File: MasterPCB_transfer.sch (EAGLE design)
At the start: 1072 parts, among them IC1 NCS21911SN2T1G, IC10 LDL1117S33R, IC11 LTC4222CUH#PBF, IC12 LTC4222CUH#PBF, IC13 LTC4222CUH#PBF, IC14 LTC4222CUH#PBF, IC15 LTC4222CUH#PBF, IC16 LTC4222CUH#PBF, IC17 LTC4222CUH#PBF, IC18 LTC4222CUH#PBF, IC19 LTC4222CUH#PBF, IC2 NCS21911SN2T1G, IC20 LTC4222CUH#PBF, IC21 LTC4222CUH#PBF, IC22 LTC4222CUH#PBF, IC23 LTC4222CUH#PBF, IC24 NCS21911SN2T1G, IC25 NCS21911SN2T1G, IC26 NCS21911SN2T1G, IC27 NCS21911SN2T1G, IC28 NCS21911SN2T1G, IC29 NCS21911SN2T1G, IC3 NCS21911SN2T1G, IC30 NCS21911SN2T1G, IC31 ADIS16500AMLZ, IC32 LTC6820IUD#PBF, IC33 CBTL01023GM,115, IC34 MAX889TESA+, IC35 NCS21911SN2T1G, IC36 NCS21911SN2T1G, IC37 NCS21911SN2T1G, IC38 ADS8588HIPM, IC39 NCS21911SN2T1G, IC4 LTC4222CUH#PBF, IC40 NCS21911SN2T1G, IC41 NCS21911SN2T1G, IC42 NCS21911SN2T1G, IC43 NCS21911SN2T1G, IC44 NCS21911SN2T1G, IC45 NCS21911SN2T1G, IC46 NCS21911SN2T1G, IC47 NCS21911SN2T1G, IC48 NCS21911SN2T1G, IC49 NCS21911SN2T1G, IC5 LP38692SDX-5.0_NOPB, IC50 NCS21911SN2T1G, IC51 ADS8588HIPM, IC52 ADS8588HIPM, IC53 NCS21911SN2T1G, IC54 NCS21911SN2T1G, IC55 NCS21911SN2T1G, IC56 NCS21911SN2T1G, IC57 NCS21911SN2T1G, IC58 NCS21911SN2T1G, IC59 NCS21911SN2T1G, IC6 LP38692SDX-5.0_NOPB, IC60 NCS21911SN2T1G, IC61 NCS21911SN2T1G, IC62 NCS21911SN2T1G, IC63 NCS21911SN2T1G, IC64 NCS21911SN2T1G, IC65 NCS21911SN2T1G, IC66 NCS21911SN2T1G, IC67 NCS21911SN2T1G, IC68 NCS21911SN2T1G, IC69 NCS21911SN2T1G, IC7 LDL1117S33R, IC70 NCS21911SN2T1G, IC71 NCS21911SN2T1G, IC72 NCS21911SN2T1G, IC73 NCS21911SN2T1G, IC74 NCS21911SN2T1G, IC75 NCS21911SN2T1G, IC76 NCS21911SN2T1G, IC77 NCS21911SN2T1G, IC78 NCS21911SN2T1G, IC79 NCS21911SN2T1G, IC8 LDL1117S33R, IC9 LP38692SDX-5.0_NOPB, J1 SAMTEC-SMM-104-02-X-DJ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

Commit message: Save point
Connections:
- removed net N$373: J6.29
- removed net N$374: J6.27
- removed net N$377: J6.19
- removed net N$381: J6.09
- removed net N$382: J6.07
- net ADIN2_8_POWER_TEMP2: no longer J6.17
- net GND: now also J6.07, J6.09, J6.17, J6.19, J6.27, J6.29, J6.31, J6.33, J6.35, J6.37, J6.39, J6.47, J6.49, J6.57, J6.59, J6.67, J6.69, J6.77, J6.79
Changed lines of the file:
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@@
 <part name="C30" library="SamacSys_Parts" library_urn="urn:adsk.eagle:library:31941355" deviceset="CS0402KRX7R8BB104" device="" package3d_urn="urn:adsk.eagle:package:34596920/2"/>
 <part name="GND22" library="supply1" library_urn="urn:adsk.eagle:library:371" deviceset="GND" device=""/>
+<part name="GND578" library="supply1" library_urn="urn:adsk.eagle:library:371" deviceset="GND" device=""/>
 </parts>
 <sheets>
@@
 <attribute name="VALUE" x="-144.78" y="2.54" size="1.778" layer="96"/>
 </instance>
+<instance part="GND578" gate="1" x="-172.72" y="0" smashed="yes">
+<attribute name="VALUE" x="-175.26" y="-2.54" size="1.778" layer="96"/>
+</instance>
 </instances>
 <busses>
@@
 <pinref part="GND542" gate="1" pin="GND"/>
 </segment>
+<segment>
+<pinref part="GND578" gate="1" pin="GND"/>
+<wire x1="-172.72" y1="2.54" x2="-175.26" y2="2.54" width="0.1524" layer="91"/>
+<wire x1="-175.26" y1="2.54" x2="-175.26" y2="7.62" width="0.1524" layer="91"/>
+<pinref part="J6" gate="G$1" pin="07"/>
+<wire x1="-175.26" y1="7.62" x2="-175.26" y2="10.16" width="0.1524" layer="91"/>
+<wire x1="-175.26" y1="10.16" x2="-175.26" y2="20.32" width="0.1524" layer="91"/>
+<wire x1="-175.26" y1="20.32" x2="-175.26" y2="22.86" width="0.1524" layer="91"/>
+<wire x1="-175.26" y1="22.86" x2="-175.26" y2="33.02" width="0.1524" layer="91"/>
+<wire x1="-175.26" y1="33.02" x2="-175.26" y2="35.56" width="0.1524" layer="91"/>
+<wire x1="-175.26" y1="35.56" x2="-175.26" y2="45.72" width="0.1524" layer="91"/>
+<wire x1="-175.26" y1="45.72" x2="-175.26" y2="48.26" width="0.1524" layer="91"/>
+<wire x1="-175.26" y1="48.26" x2="-175.26" y2="58.42" width="0.1524" layer="91"/>
+<wire x1="-175.26" y1="58.42" x2="-175.26" y2="60.96" width="0.1524" layer="91"/>
+<wire x1="-175.26" y1="60.96" x2="-175.26" y2="63.5" width="0.1524" layer="91"/>
+<wire x1="-175.26" y1="63.5" x2="-175.26" y2="66.04" width="0.1524" layer="91"/>
+<wire x1="-175.26" y1="66.04" x2="-175.26" y2="68.58" width="0.1524" layer="91"/>
+<wire x1="-175.26" y1="68.58" x2="-175.26" y2="71.12" width="0.1524" layer="91"/>
+<wire x1="-175.26" y1="71.12" x2="-175.26" y2="73.66" width="0.1524" layer="91"/>
+<wire x1="-175.26" y1="73.66" x2="-175.26" y2="83.82" width="0.1524" layer="91"/>
+<wire x1="-175.26" y1="83.82" x2="-175.26" y2="86.36" width="0.1524" layer="91"/>
+<wire x1="-175.26" y1="86.36" x2="-175.26" y2="96.52" width="0.1524" layer="91"/>
+<wire x1="-175.26" y1="96.52" x2="-175.26" y2="99.06" width="0.1524" layer="91"/>
+<wire x1="-149.86" y1="99.06" x2="-175.26" y2="99.06" width="0.1524" layer="91"/>
+<pinref part="J6" gate="G$1" pin="09"/>
+<wire x1="-149.86" y1="96.52" x2="-175.26" y2="96.52" width="0.1524" layer="91"/>
+<junction x="-175.26" y="96.52"/>
+<pinref part="J6" gate="G$1" pin="17"/>
+<wire x1="-149.86" y1="86.36" x2="-175.26" y2="86.36" width="0.1524" layer="91"/>
+<junction x="-175.26" y="86.36"/>
+<pinref part="J6" gate="G$1" pin="19"/>
+<wire x1="-149.86" y1="83.82" x2="-175.26" y2="83.82" width="0.1524" layer="91"/>
+<junction x="-175.26" y="83.82"/>
+<pinref part="J6" gate="G$1" pin="27"/>
+<wire x1="-149.86" y1="73.66" x2="-175.26" y2="73.66" width="0.1524" layer="91"/>
+<junction x="-175.26" y="73.66"/>
+<pinref part="J6" gate="G$1" pin="29"/>
+<wire x1="-149.86" y1="71.12" x2="-175.26" y2="71.12" width="0.1524" layer="91"/>
+<junction x="-175.26" y="71.12"/>
+<pinref part="J6" gate="G$1" pin="31"/>
+<wire x1="-149.86" y1="68.58" x2="-175.26" y2="68.58" width="0.1524" layer="91"/>
+<junction x="-175.26" y="68.58"/>
+<pinref part="J6" gate="G$1" pin="33"/>
+<wire x1="-149.86" y1="66.04" x2="-175.26" y2="66.04" width="0.1524" layer="91"/>
+<junction x="-175.26" y="66.04"/>
+<pinref part="J6" gate="G$1" pin="35"/>
+<wire x1="-149.86" y1="63.5" x2="-175.26" y2="63.5" width="0.1524" layer="91"/>
+<junction x="-175.26" y="63.5"/>
+<pinref part="J6" gate="G$1" pin="37"/>
+<wire x1="-149.86" y1="60.96" x2="-175.26" y2="60.96" width="0.1524" layer="91"/>
+<junction x="-175.26" y="60.96"/>
+<pinref part="J6" gate="G$1" pin="39"/>
+<wire x1="-149.86" y1="58.42" x2="-175.26" y2="58.42" width="0.1524" layer="91"/>
+<junction x="-175.26" y="58.42"/>
+<pinref part="J6" gate="G$1" pin="47"/>
+<wire x1="-149.86" y1="48.26" x2="-175.26" y2="48.26" width="0.1524" layer="91"/>
+<junction x="-175.26" y="48.26"/>
+<pinref part="J6" gate="G$1" pin="49"/>
+<wire x1="-149.86" y1="45.72" x2="-175.26" y2="45.72" width="0.1524" layer="91"/>
+<junction x="-175.26" y="45.72"/>
+<pinref part="J6" gate="G$1" pin="57"/>
+<wire x1="-149.86" y1="35.56" x2="-175.26" y2="35.56" width="0.1524" layer="91"/>
+<junction x="-175.26" y="35.56"/>
+<pinref part="J6" gate="G$1" pin="59"/>
+<wire x1="-149.86" y1="33.02" x2="-175.26" y2="33.02" width="0.1524" layer="91"/>
+<junction x="-175.26" y="33.02"/>
+<pinref part="J6" gate="G$1" pin="67"/>
+<wire x1="-149.86" y1="22.86" x2="-175.26" y2="22.86" width="0.1524" layer="91"/>
+<junction x="-175.26" y="22.86"/>
+<pinref part="J6" gate="G$1" pin="69"/>
+<wire x1="-149.86" y1="20.32" x2="-175.26" y2="20.32" width="0.1524" layer="91"/>
+<junction x="-175.26" y="20.32"/>
+<pinref part="J6" gate="G$1" pin="77"/>
+<wire x1="-149.86" y1="10.16" x2="-175.26" y2="10.16" width="0.1524" layer="91"/>
+<junction x="-175.26" y="10.16"/>
+<pinref part="J6" gate="G$1" pin="79"/>
+<wire x1="-149.86" y1="7.62" x2="-175.26" y2="7.62" width="0.1524" layer="91"/>
+<junction x="-175.26" y="7.62"/>
+</segment>
 </net>
 <net name="DIFF1_P" class="0">
@@
 </segment>
 <segment>
-<wire x1="-152.4" y1="86.36" x2="-149.86" y2="86.36" width="0.1524" layer="91"/>
-<pinref part="J6" gate="G$1" pin="17"/>
-</segment>
-<segment>
 <pinref part="J6" gate="G$1" pin="16"/>
 <wire x1="-121.92" y1="88.9" x2="-124.46" y2="88.9" width="0.1524" layer="91"/>
@@
 </segment>
 </net>
-<net name="N$381" class="0">
-<segment>
-<wire x1="-152.4" y1="96.52" x2="-149.86" y2="96.52" width="0.1524" layer="91"/>
-<pinref part="J6" gate="G$1" pin="09"/>
-</segment>
-</net>
-<net name="N$382" class="0">
-<segment>
-<wire x1="-152.4" y1="99.06" x2="-149.86" y2="99.06" width="0.1524" layer="91"/>
-<pinref part="J6" gate="G$1" pin="07"/>
-</segment>
-</net>
-<net name="N$377" class="0">
-<segment>
-<wire x1="-152.4" y1="83.82" x2="-149.86" y2="83.82" width="0.1524" layer="91"/>
-<pinref part="J6" gate="G$1" pin="19"/>
-</segment>
-</net>
-<net name="N$373" class="0">
-<segment>
-<wire x1="-152.4" y1="71.12" x2="-149.86" y2="71.12" width="0.1524" layer="91"/>
-<pinref part="J6" gate="G$1" pin="29"/>
-</segment>
-</net>
-<net name="N$374" class="0">
-<segment>
-<wire x1="-152.4" y1="73.66" x2="-149.86" y2="73.66" width="0.1524" layer="91"/>
-<pinref part="J6" gate="G$1" pin="27"/>
-</segment>
-</net>

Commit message: Save point
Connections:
- removed net PG7: J12.23
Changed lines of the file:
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@@
-</segment>
-</net>
-<net name="PG7" class="0">
-<segment>
-<wire x1="63.5" y1="-48.26" x2="66.04" y2="-48.26" width="0.1524" layer="91"/>
-<label x="60.96" y="-45.72" size="1.778" layer="95" rot="R180"/>
-<pinref part="J12" gate="G$1" pin="23"/>
 </segment>
 </net>

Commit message: Save point
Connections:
- removed net PB13: J14.67
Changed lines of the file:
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@@
 </busses>
 <nets>
-<net name="PB13" class="0">
-<segment>
-<wire x1="-5.08" y1="-104.14" x2="-2.54" y2="-104.14" width="0.1524" layer="91"/>
-<label x="-7.62" y="-104.14" size="1.778" layer="95" rot="MR0"/>
-<pinref part="J14" gate="G$1" pin="67"/>
-</segment>
-</net>
 <net name="5V_CONNECTOR" class="0">
 <segment>

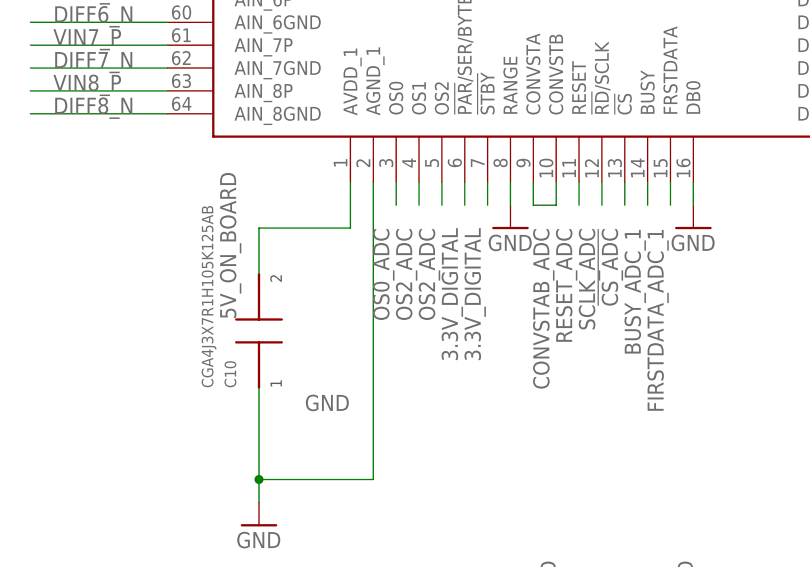
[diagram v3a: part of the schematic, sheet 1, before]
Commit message: New board shape
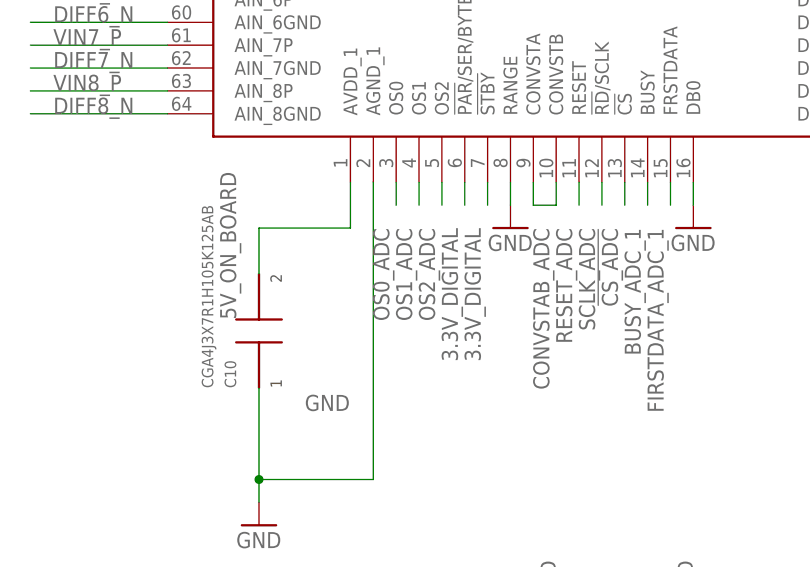
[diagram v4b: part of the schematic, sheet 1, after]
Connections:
- net OS1_ADC: now also IC51.OS1
- net OS2_ADC: no longer IC51.OS1
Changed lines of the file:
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@@
 <net name="OS2_ADC" class="0">
-<segment>
-<pinref part="IC51" gate="G$1" pin="OS1"/>
-<wire x1="586.74" y1="345.44" x2="586.74" y2="347.98" width="0.1524" layer="91"/>
-<label x="584.2" y="342.9" size="1.778" layer="95" rot="R270"/>
-</segment>
 <segment>
 <pinref part="IC51" gate="G$1" pin="OS2"/>
@@
 <label x="589.28" y="104.14" size="1.778" layer="95" rot="R270"/>
 </segment>
-</net>
+<segment>
+<pinref part="IC51" gate="G$1" pin="OS1"/>
+<wire x1="586.74" y1="345.44" x2="586.74" y2="347.98" width="0.1524" layer="91"/>
+<label x="584.2" y="342.9" size="1.778" layer="95" rot="R270"/>
+</segment>
+</net>

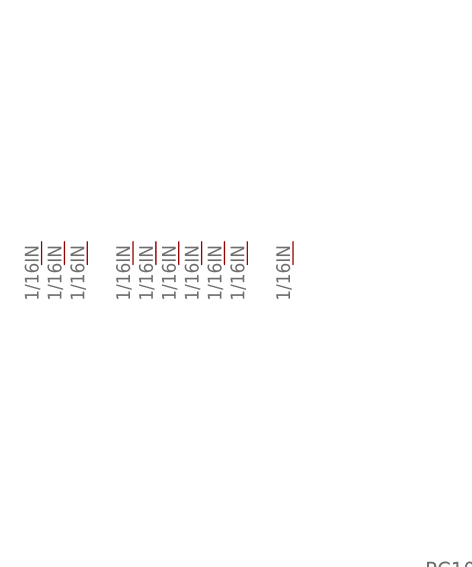
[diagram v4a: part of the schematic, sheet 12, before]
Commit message: New board shape
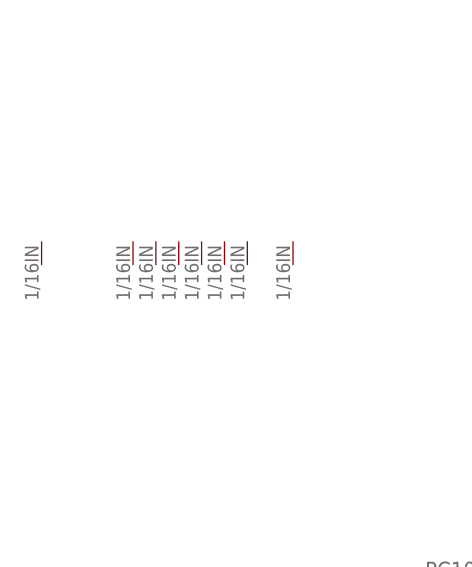
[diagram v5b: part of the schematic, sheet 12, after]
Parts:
- removed U$12, U$13: THROUGH_HOLE, SamacSys_Parts:THROUGH_HOLE
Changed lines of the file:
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@@
 <part name="U$9" library="SamacSys_Parts" library_urn="urn:adsk.eagle:library:31941355" deviceset="THROUGH_HOLE" device="" package3d_urn="urn:adsk.eagle:package:35094096/3"/>
 <part name="U$10" library="SamacSys_Parts" library_urn="urn:adsk.eagle:library:31941355" deviceset="THROUGH_HOLE" device="" package3d_urn="urn:adsk.eagle:package:35094096/3"/>
-<part name="U$12" library="SamacSys_Parts" library_urn="urn:adsk.eagle:library:31941355" deviceset="THROUGH_HOLE" device="" package3d_urn="urn:adsk.eagle:package:35094096/3"/>
-<part name="U$13" library="SamacSys_Parts" library_urn="urn:adsk.eagle:library:31941355" deviceset="THROUGH_HOLE" device="" package3d_urn="urn:adsk.eagle:package:35094096/3"/>
 <part name="U$14" library="SamacSys_Parts" library_urn="urn:adsk.eagle:library:31941355" deviceset="THROUGH_HOLE" device="" package3d_urn="urn:adsk.eagle:package:35094096/3"/>
 <part name="U$15" library="SamacSys_Parts" library_urn="urn:adsk.eagle:library:31941355" deviceset="THROUGH_HOLE" device="" package3d_urn="urn:adsk.eagle:package:35094096/3"/>
@@
 <instance part="U$9" gate="G$1" x="-40.64" y="132.08" smashed="yes"/>
 <instance part="U$10" gate="G$1" x="-43.18" y="132.08" smashed="yes"/>
-<instance part="U$12" gate="G$1" x="-48.26" y="132.08" smashed="yes"/>
-<instance part="U$13" gate="G$1" x="-50.8" y="132.08" smashed="yes"/>
 <instance part="U$14" gate="G$1" x="-53.34" y="132.08" smashed="yes"/>
 <instance part="U$15" gate="G$1" x="-25.4" y="132.08" smashed="yes"/>

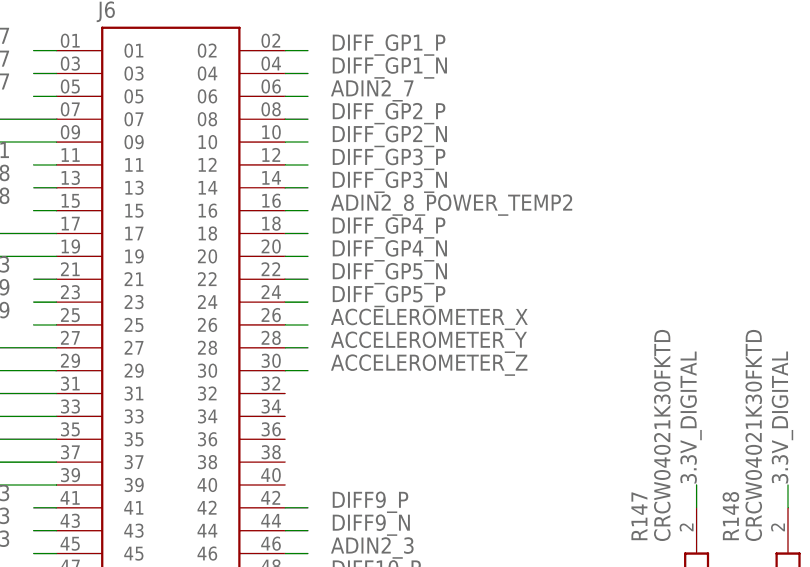
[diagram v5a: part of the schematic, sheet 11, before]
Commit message: Routed analog filters
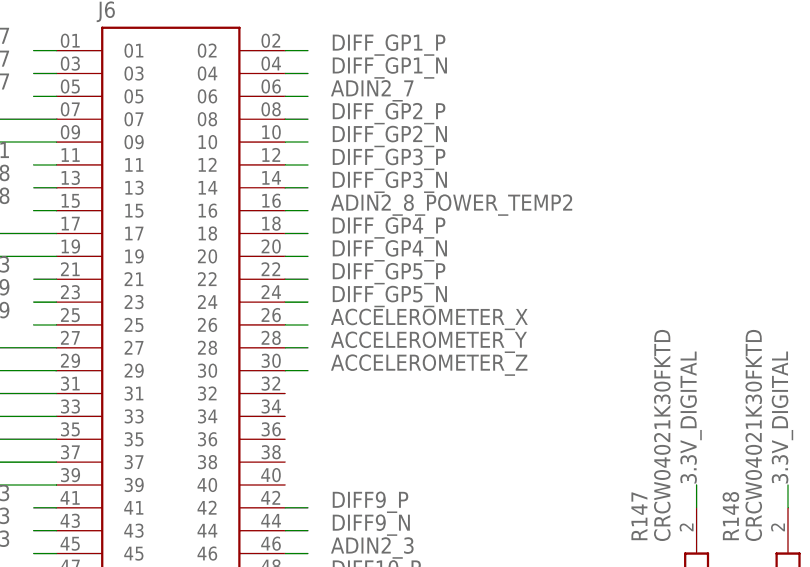
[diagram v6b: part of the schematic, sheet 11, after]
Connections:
- net DIFF3_N: no longer C259.2
- net DIFF_GP3_N: now also C259.2
- net DIFF_GP5_N: now also J6.24; no longer J6.22
- net DIFF_GP5_P: now also J6.22; no longer J6.24
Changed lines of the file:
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@@
 <pinref part="IC52" gate="G$1" pin="AIN_3GND"/>
 </segment>
+<segment>
+<pinref part="C259" gate="G$1" pin="2"/>
+<wire x1="60.96" y1="147.32" x2="60.96" y2="144.78" width="0.1524" layer="91"/>
+<wire x1="60.96" y1="144.78" x2="5.08" y2="144.78" width="0.1524" layer="91"/>
+<label x="-5.08" y="147.32" size="1.778" layer="95"/>
+</segment>
 </net>
 <net name="GP_4_P" class="0">
@@
 </segment>
 </net>
-<net name="DIFF3_N" class="0">
-<segment>
-<pinref part="C259" gate="G$1" pin="2"/>
-<wire x1="60.96" y1="147.32" x2="60.96" y2="144.78" width="0.1524" layer="91"/>
-<wire x1="60.96" y1="144.78" x2="5.08" y2="144.78" width="0.1524" layer="91"/>
-<label x="-5.08" y="147.32" size="1.778" layer="95"/>
-</segment>
-</net>
 </nets>
 </sheet>
@@
 </segment>
 <segment>
-<wire x1="-121.92" y1="78.74" x2="-124.46" y2="78.74" width="0.1524" layer="91"/>
-<label x="-119.38" y="78.74" size="1.778" layer="95"/>
-<pinref part="J6" gate="G$1" pin="24"/>
+<wire x1="-121.92" y1="81.28" x2="-124.46" y2="81.28" width="0.1524" layer="91"/>
+<label x="-119.38" y="81.28" size="1.778" layer="95"/>
+<pinref part="J6" gate="G$1" pin="22"/>
 </segment>
 </net>
@@
 </segment>
 <segment>
-<wire x1="-121.92" y1="81.28" x2="-124.46" y2="81.28" width="0.1524" layer="91"/>
-<label x="-119.38" y="81.28" size="1.778" layer="95"/>
-<pinref part="J6" gate="G$1" pin="22"/>
+<wire x1="-121.92" y1="78.74" x2="-124.46" y2="78.74" width="0.1524" layer="91"/>
+<label x="-119.38" y="78.74" size="1.778" layer="95"/>
+<pinref part="J6" gate="G$1" pin="24"/>
 </segment>
 </net>
